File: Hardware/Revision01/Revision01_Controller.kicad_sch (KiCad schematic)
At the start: 8 parts, among them U1 NUCLEO-L476RG

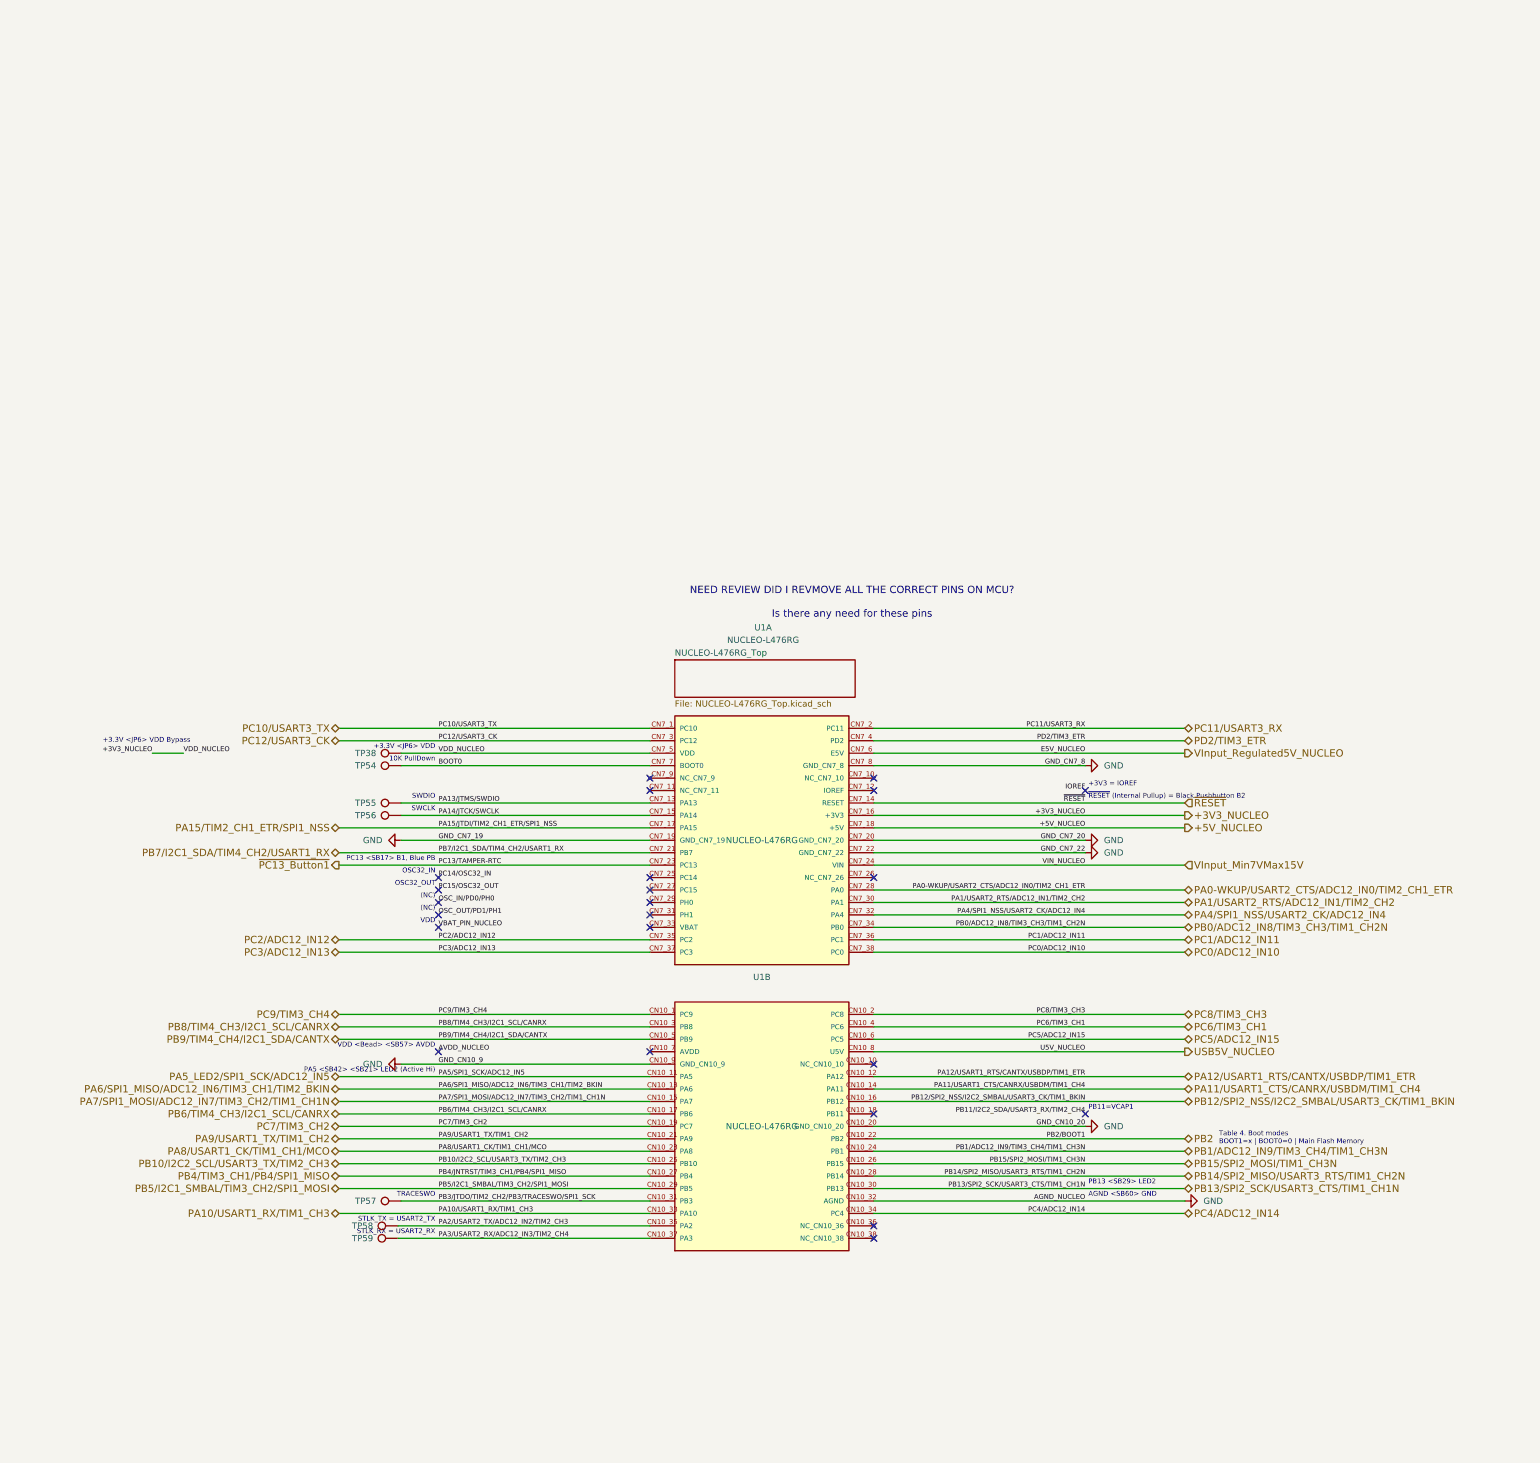
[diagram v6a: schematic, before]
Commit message: CREATE STM32CUBEIDE file to verify all ports Check over CONTROLLER SHEET Improve annotation ordering Move testpoints out of controller sheet
Still performering ERC check
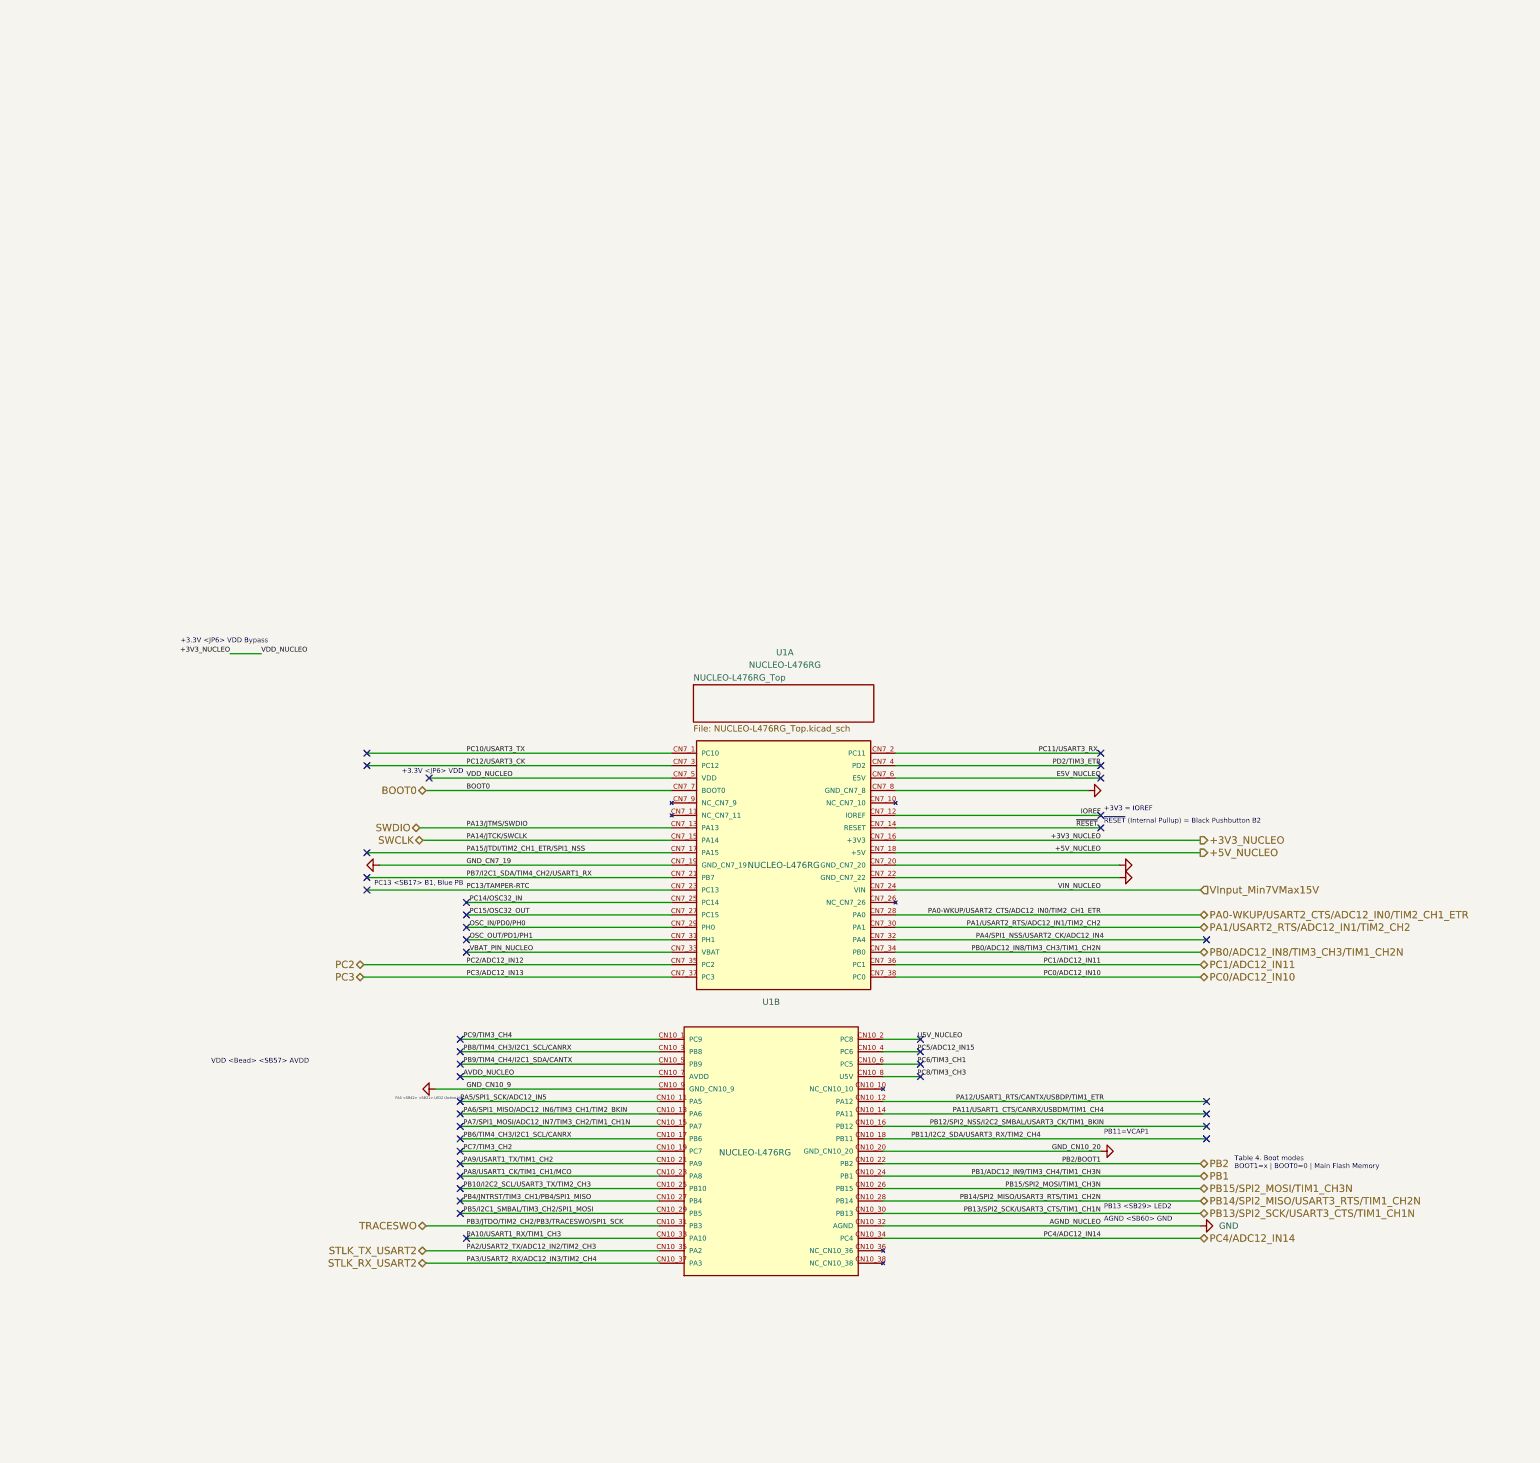
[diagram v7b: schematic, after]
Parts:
- removed TP38, TP54, TP55, TP56, TP57, TP58, TP59: TestPoint, TestPoint:TestPoint_THTPad_1.0x1.0mm_Drill0.5mm, symbol Connector:TestPoint
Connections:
- net USB5V_NUCLEO is gone; now on net PC8/TIM3_CH3: U1.CN10_8 (U5V)
- net AVDD_NUCLEO: now also U1.CN10_7 (AVDD)
- net IOREF: now also U1.CN7_12 (IOREF)
- net OSC_IN/PD0/PH0: now also U1.CN7_29 (PH0)
- net OSC_OUT/PD1/PH1: now also U1.CN7_31 (PH1)
- net PB11/I2C2_SDA/USART3_RX/TIM2_CH4: now also U1.CN10_18 (PB11)
- net PC14/OSC32_IN: now also U1.CN7_25 (PC14)
- net PC15/OSC32_OUT: now also U1.CN7_27 (PC15)
- net PC5/ADC12_IN15: now also U1.CN10_4 (PC6); no longer U1.CN10_6 (PC5)
- net PC6/TIM3_CH1: now also U1.CN10_6 (PC5); no longer U1.CN10_4 (PC6)
- net PC8/TIM3_CH3: no longer U1.CN10_2 (PC8)
- net VBAT_PIN_NUCLEO: now also U1.CN7_33 (VBAT)
- net PA13/JTMS/SWDIO renamed SWDIO
- net PA14/JTCK/SWCLK renamed SWCLK
- net PA15/TIM2_CH1_ETR/SPI1_NSS renamed PA15/JTDI/TIM2_CH1_ETR/SPI1_NSS
- net PA2/USART2_TX/ADC12_IN2/TIM2_CH3 renamed STLK_TX_USART2
- net PA3/USART2_RX/ADC12_IN3/TIM2_CH4 renamed STLK_RX_USART2
- net PA5_LED2/SPI1_SCK/ADC12_IN5 renamed PA5/SPI1_SCK/ADC12_IN5
- net PB1/ADC12_IN9/TIM3_CH4/TIM1_CH3N renamed PB1
- net PB3/JTDO/TIM2_CH2/PB3/TRACESWO/SPI1_SCK renamed TRACESWO
- net PB4/TIM3_CH1/PB4/SPI1_MISO renamed PB4/JNTRST/TIM3_CH1/PB4/SPI1_MISO
- net PC2/ADC12_IN12 renamed PC2
- net PC3/ADC12_IN13 renamed PC3
- net VInput_Regulated5V_NUCLEO renamed E5V_NUCLEO
- net ~{PC13_Button1} renamed PC13/TAMPER-RTC
- new net U5V_NUCLEO: U1.CN10_2 (PC8)
- no-connect marks 23 -> 40
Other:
- note removed: "(NC)"
- note removed: "10K PullDown"
- note removed: "NEED REVIEW DID I REVMOVE ALL THE CORRECT PINS ON MCU? Is there any need for these pins"
- note removed: "OSC32_IN"
- note removed: "OSC32_OUT"
- note removed: "STLK_RX = USART2_RX"
- note removed: "STLK_TX = USART2_TX"
- note removed: "SWCLK"
- note removed: "SWDIO"
- note removed: "TRACESWO"
- note removed: "VDD"
- moved on the sheet: U1A, U1B

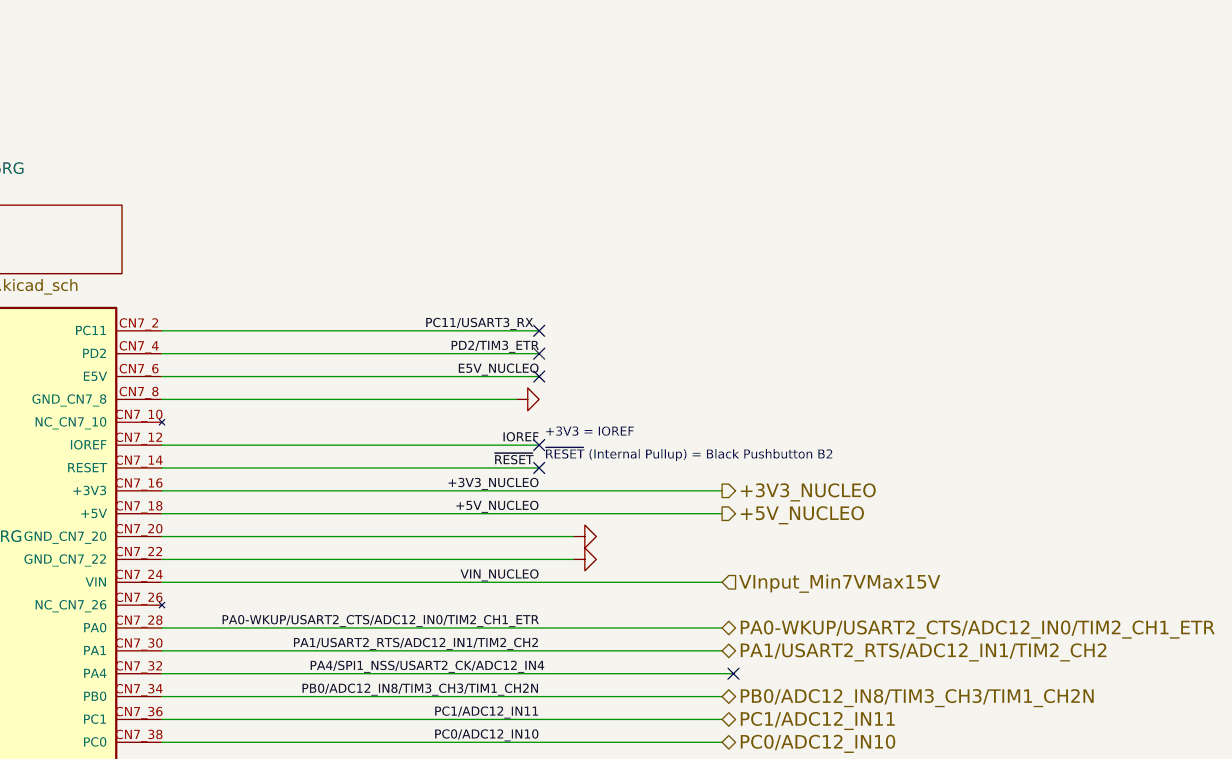
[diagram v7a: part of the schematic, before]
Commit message: Added new LDO to fit into battery range that feeds into MCU, make sure to remove power jumper wire before connecting. Completed ERC check
Still have to put on footprints for some components when doing PCB layout
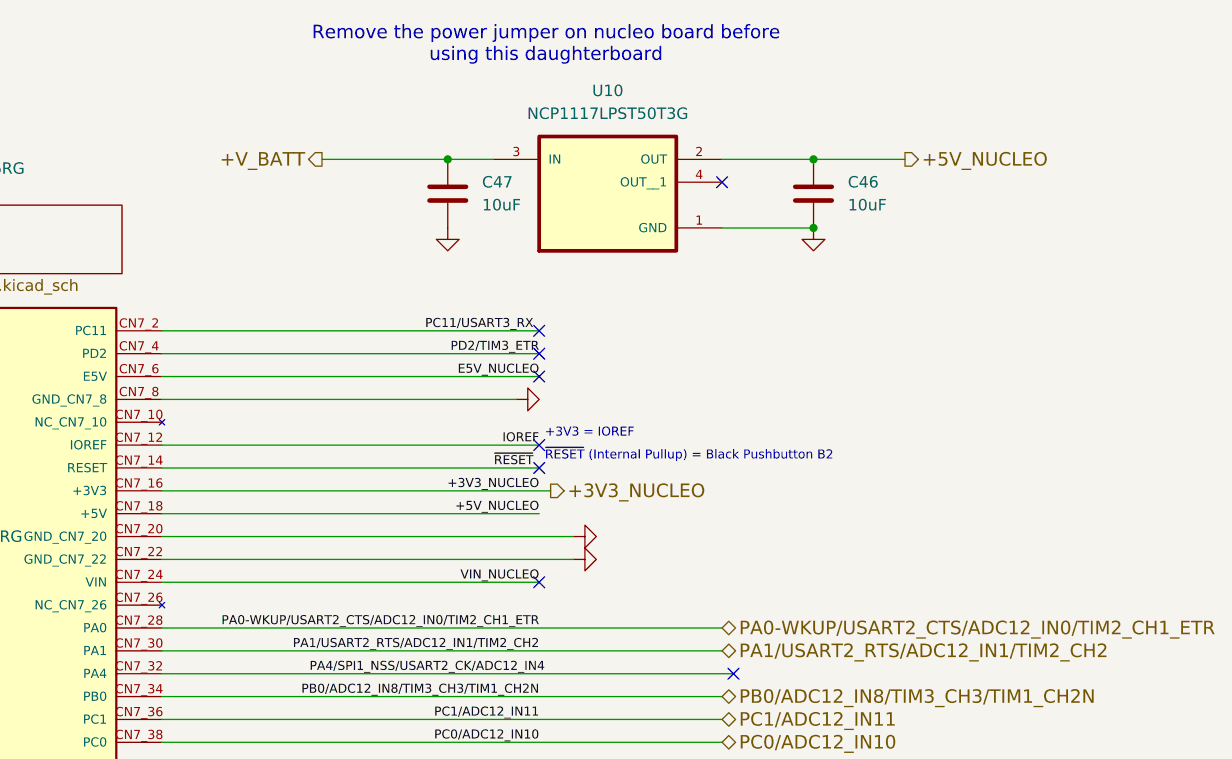
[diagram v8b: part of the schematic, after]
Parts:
- added C46, C47: 10uF, Capacitor_SMD:C_1206_3216Metric, symbol Device:C
- added U10: NCP1117LPST50T3G, NCP1117LPST50T3G:SOT230P700X180-4N, symbol NCP1117LPST50T3G:NCP1117LPST50T3G
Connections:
- net +5V_NUCLEO: now also C46.1, U10.2 (OUT)
- net GND: now also C46.2, C47.2, U10.1 (GND)
- net VInput_Min7VMax15V renamed VIN_NUCLEO
- new net +V_BATT: C47.1, U10.3 (IN)
- no-connect marks 40 -> 42
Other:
- note added: "Remove the power jumper on nucleo board before using this daughterboard"
